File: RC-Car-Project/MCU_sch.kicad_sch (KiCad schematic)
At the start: 0 parts

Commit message: Add libraries and components in schs
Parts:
- added U7: STM32H743VGTx, Package_QFP:LQFP-100_14x14mm_P0.5mm, symbol MCU_ST_STM32H7:STM32H743VGTx
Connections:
- new net: U7.10 (VSS), U7.26 (VSS), U7.49 (VSS), U7.74 (VSS), U7.99 (VSS)

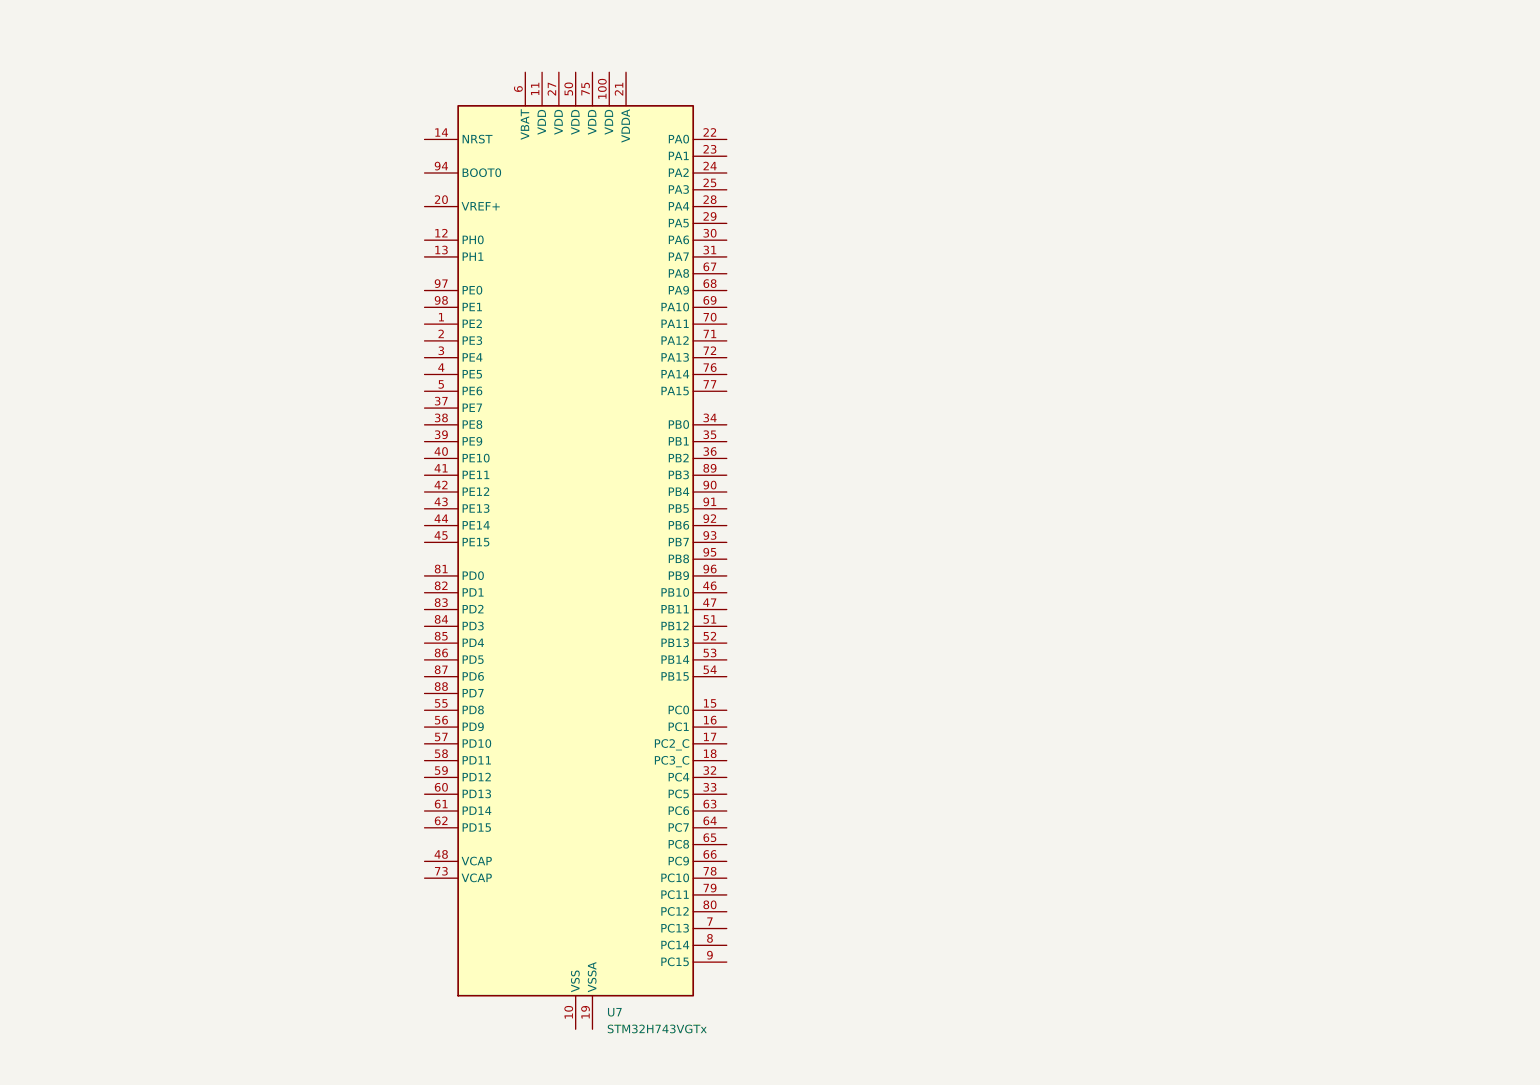
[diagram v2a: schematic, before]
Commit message: Added Basic Schematic + STM32 Project config. TODO: Component value selection + double check all connections.
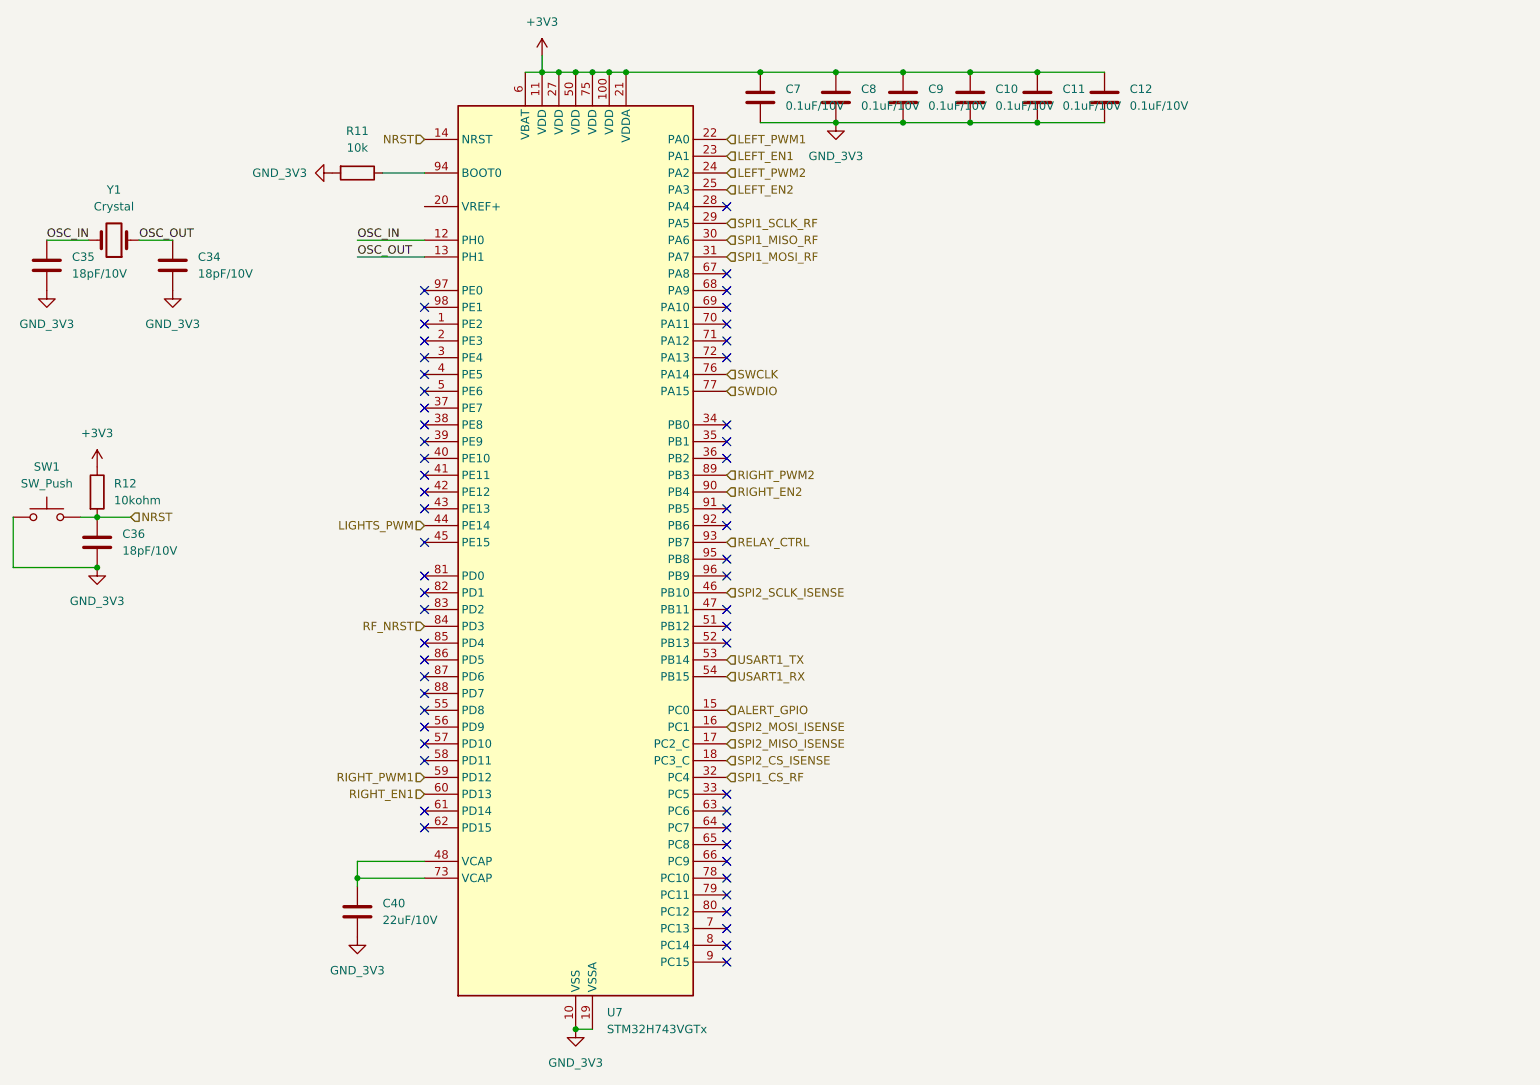
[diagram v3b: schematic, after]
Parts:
- added C10, C11, C12, C7, C8, C9: 0.1uF/10V, symbol Device:C
- added C34, C35, C36: 18pF/10V, symbol Device:C
- added C40: 22uF/10V, symbol Device:C
- added R11: 10k, symbol Device:R
- added R12: 10kohm, symbol Device:R
- added SW1: SW_Push, symbol Switch:SW_Push
- added Y1: Crystal, symbol Device:Crystal
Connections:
- net GND_3V3: now reaches U7.10 (VSS), U7.26 (VSS), U7.49 (VSS), U7.74 (VSS), U7.99 (VSS)
- net GND_3V3: now also U7.19 (VSSA), C10.2, C11.2, C12.2, C34.2, C35.2, C36.2, C40.2, C7.2, C8.2, C9.2, R11.2, SW1.1
- net +3V3: now reaches U7.100 (VDD)
- net +3V3: now also U7.11 (VDD), U7.21 (VDDA), U7.27 (VDD), U7.50 (VDD), U7.6 (VBAT), U7.75 (VDD), C10.1, C11.1, C12.1, C7.1, C8.1, C9.1, R12.1
- net OSC_IN: now reaches U7.12 (PH0)
- net OSC_IN: now also C35.1, Y1.2
- net OSC_OUT: now reaches U7.13 (PH1)
- net OSC_OUT: now also C34.1, Y1.1
- net NRST: now reaches U7.14 (NRST)
- net NRST: now also C36.1, R12.2, SW1.2
- net ALERT_GPIO: now reaches U7.15 (PC0)
- net SPI2_MOSI_ISENSE: now reaches U7.16 (PC1)
- net SPI2_MISO_ISENSE: now reaches U7.17 (PC2_C)
- net SPI2_CS_ISENSE: now reaches U7.18 (PC3_C)
- net LEFT_PWM1: now reaches U7.22 (PA0)
- net LEFT_EN1: now reaches U7.23 (PA1)
- net LEFT_PWM2: now reaches U7.24 (PA2)
- net LEFT_EN2: now reaches U7.25 (PA3)
- net SPI1_SCLK_RF: now reaches U7.29 (PA5)
- net SPI1_MISO_RF: now reaches U7.30 (PA6)
- net SPI1_MOSI_RF: now reaches U7.31 (PA7)
- net SPI1_CS_RF: now reaches U7.32 (PC4)
- net LIGHTS_PWM: now reaches U7.44 (PE14)
- net SPI2_SCLK_ISENSE: now reaches U7.46 (PB10)
- net at U7.48 (VCAP): now also U7.73 (VCAP), C40.1
- net USART1_TX: now reaches U7.53 (PB14)
- net USART1_RX: now reaches U7.54 (PB15)
- net RIGHT_PWM1: now reaches U7.59 (PD12)
- net RIGHT_EN1: now reaches U7.60 (PD13)
- net SWCLK: now reaches U7.76 (PA14)
- net SWDIO: now reaches U7.77 (PA15)
- net RF_NRST: now reaches U7.84 (PD3)
- net RIGHT_PWM2: now reaches U7.89 (PB3)
- net RIGHT_EN2: now reaches U7.90 (PB4)
- net RELAY_CTRL: now reaches U7.93 (PB7)
- net at U7.94 (BOOT0): now also R11.1
- no-connect marks 0 -> 56

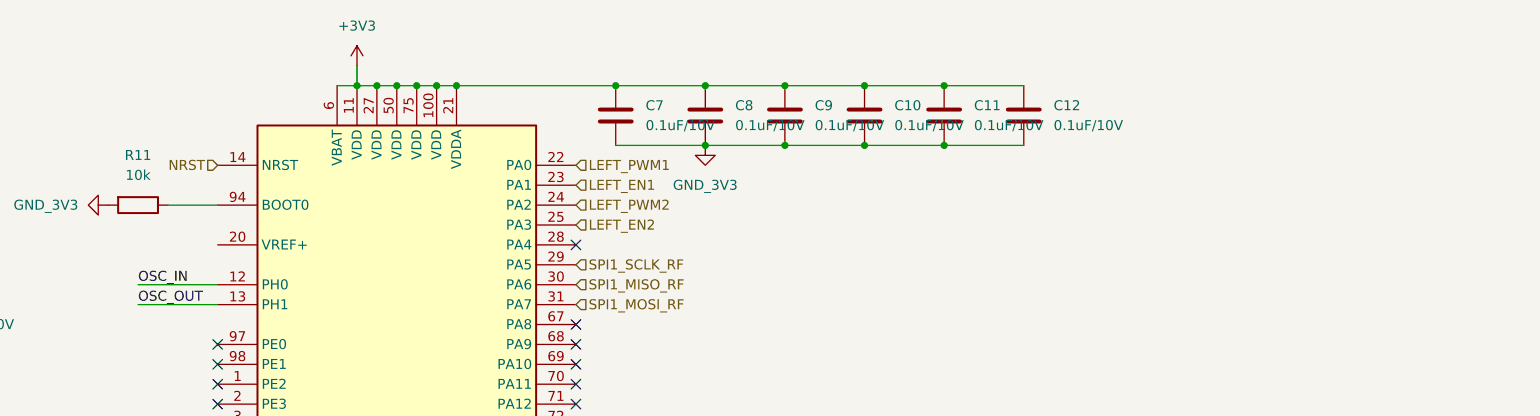
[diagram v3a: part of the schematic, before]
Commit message: Added footprints + final parts. (Need to finish buck converter next)
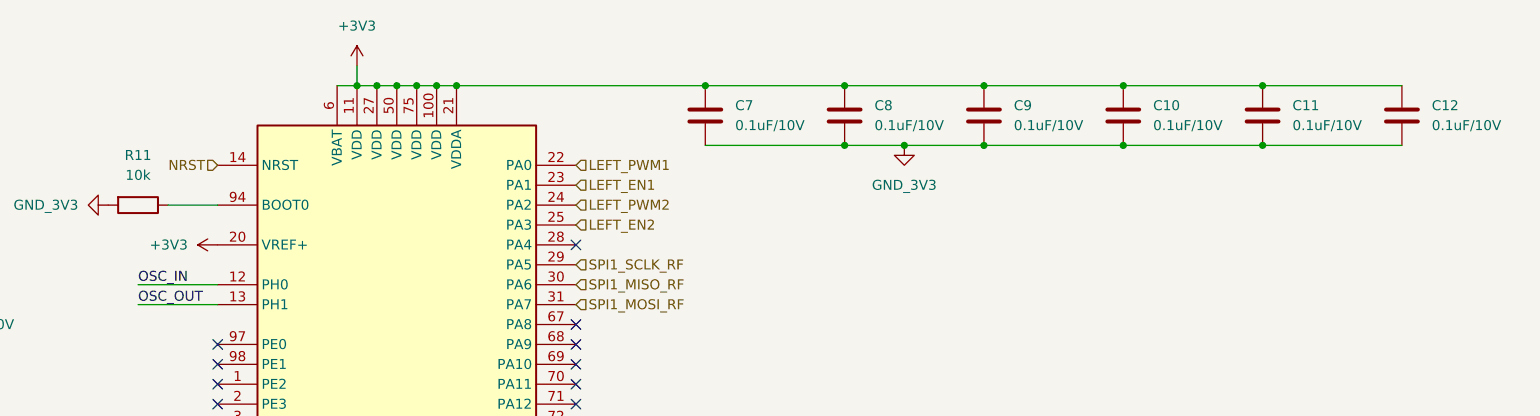
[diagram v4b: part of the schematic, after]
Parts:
- C10, C11, C12, C34, C35, C36, C7, C8, C9: footprint (none) -> Capacitor_SMD:C_0201_0603Metric
- R11, R12: footprint (none) -> Resistor_SMD:R_0201_0603Metric
- SW1: footprint (none) -> Button_Switch_THT:SW_SPST_Omron_B3F-40xx
- Y1: footprint (none) -> Crystal:Crystal_SMD_Abracon_ABM3-2Pin_5.0x3.2mm
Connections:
- net +3V3: now also U7.20 (VREF+)
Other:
- moved on the sheet: C10, C11, C12, C7, C8, C9

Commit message: Finished Buck
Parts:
- added C21: 2.2uF/10V, Capacitor_SMD:C_0201_0603Metric, symbol Device:C
- C40: value 22uF/10V -> 2.2uF/10V; footprint (none) -> Capacitor_SMD:C_0201_0603Metric
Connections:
- net GND_3V3: now also C21.2
- net at C40.1, U7.73 (VCAP): no longer U7.48 (VCAP)
- new net: C21.1, U7.48 (VCAP)
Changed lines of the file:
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@@
-	)
-	(junction
-		(at 106.68 143.51)
-		(diameter 0)
-		(color 0 0 0 0)
 	)
 	(junction
@@
 	(wire
 		(pts
-			(xy 106.68 140.97) (xy 106.68 143.51)
-		)
-		(stroke
-			(width 0)
-			(type default)
-		)
-	)
-	(wire
-		(pts
-			(xy 116.84 140.97) (xy 106.68 140.97)
+			(xy 88.9 140.97) (xy 116.84 140.97)
 		)
 		(stroke
@@
 		(pts
 			(xy 106.68 46.99) (xy 116.84 46.99)
+		)
+		(stroke
+			(width 0)
+			(type default)
+		)
+	)
+	(wire
+		(pts
+			(xy 88.9 144.78) (xy 88.9 140.97)
 		)
 		(stroke
@@
 			)
 		)
-		(property "Value" "22uF/10V"
+		(property "Value" "2.2uF/10V"
 			(at 110.49 149.8599 0)
 			(effects
@@
 			)
 		)
-		(property "Footprint" ""
+		(property "Footprint" "Capacitor_SMD:C_0201_0603Metric"
 			(at 107.6452 152.4 0)
 			(effects
@@
 	)
 	(symbol
+		(lib_id "Device:C")
+		(at 88.9 148.59 0)
+		(unit 1)
+		(exclude_from_sim no)
+		(in_bom yes)
+		(on_board yes)
+		(dnp no)
+		(fields_autoplaced yes)
+		(property "Reference" "C21"
+			(at 92.71 147.3199 0)
+			(effects
+				(font
+					(size 1.27 1.27)
+				)
+				(justify left)
+			)
+		)
+		(property "Value" "2.2uF/10V"
+			(at 92.71 149.8599 0)
+			(effects
+				(font
+					(size 1.27 1.27)
+				)
+				(justify left)
+			)
+		)
+		(property "Footprint" "Capacitor_SMD:C_0201_0603Metric"
+			(at 89.8652 152.4 0)
+			(effects
+				(font
+					(size 1.27 1.27)
+				)
+				(hide yes)
+			)
+		)
+		(property "Datasheet" "~"
+			(at 88.9 148.59 0)
+			(effects
+				(font
+					(size 1.27 1.27)
+				)
+				(hide yes)
+			)
+		)
+		(property "Description" "Unpolarized capacitor"
+			(at 88.9 148.59 0)
+			(effects
+				(font
+					(size 1.27 1.27)
+				)
+				(hide yes)
+			)
+		)
+		(pin "1"
+		)
+		(pin "2"
+		)
+		(instances
+			(project "RC-Car-Project"
+				(path "/ba870fd1-751d-4755-8e1a-1ea86ca9e2f6/a5d771ee-9d16-4fd4-bdeb-bf0012c0663a"
+					(reference "C21")
+					(unit 1)
+				)
+			)
+		)
+	)
+	(symbol
 		(lib_id "power:GND")
 		(at 106.68 152.4 0)
@@
 					(unit 1)
 				)
+			)
+		)
+	)
+	(symbol
+		(lib_id "power:GND")
+		(at 88.9 152.4 0)
+		(unit 1)
+		(exclude_from_sim no)
+		(in_bom yes)
+		(on_board yes)
+		(dnp no)
+		(fields_autoplaced yes)
+		(property "Reference" "#PWR018"
+			(at 88.9 158.75 0)
+			(effects
+				(font
+					(size 1.27 1.27)
+				)
+				(hide yes)
+			)
+		)
+		(property "Value" "GND_3V3"
+			(at 88.9 157.48 0)
+			(effects
+				(font
+					(size 1.27 1.27)
+				)
+			)
+		)
+		(property "Footprint" ""
+			(at 88.9 152.4 0)
+			(effects
+				(font
+					(size 1.27 1.27)
+				)
+				(hide yes)
+			)
+		)
+		(property "Datasheet" ""
+			(at 88.9 152.4 0)
+			(effects
+				(font
+					(size 1.27 1.27)
+				)
+				(hide yes)
+			)
+		)
+		(property "Description" "Power symbol creates a global label with name \"GND\" , ground"
+			(at 88.9 152.4 0)
+			(effects
+				(font
+					(size 1.27 1.27)
+				)
+				(hide yes)
+			)
+		)
+		(pin "1"
+		)
+		(instances
+			(project "RC-Car-Project"
+				(path "/ba870fd1-751d-4755-8e1a-1ea86ca9e2f6/a5d771ee-9d16-4fd4-bdeb-bf0012c0663a"
+					(reference "#PWR018")
+					(unit 1)
+				)
